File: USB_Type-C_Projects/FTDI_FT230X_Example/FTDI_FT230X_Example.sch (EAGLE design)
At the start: 52 parts, among them J1 105450-0101, J2 MF-CON-2.54mm-01x03, J3 MF-CON-2.54mm-01x02, J4 MF-CON-2.54mm-01x05, J5 MF-CON-2.54mm-01x03, J6 MF-CON-2.54mm-01x05, U1 FT230XQ-R, U2 IP4234CZ6,125, U3 IRLML6401TRPBF, U4 NCP1117LPST33T3G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

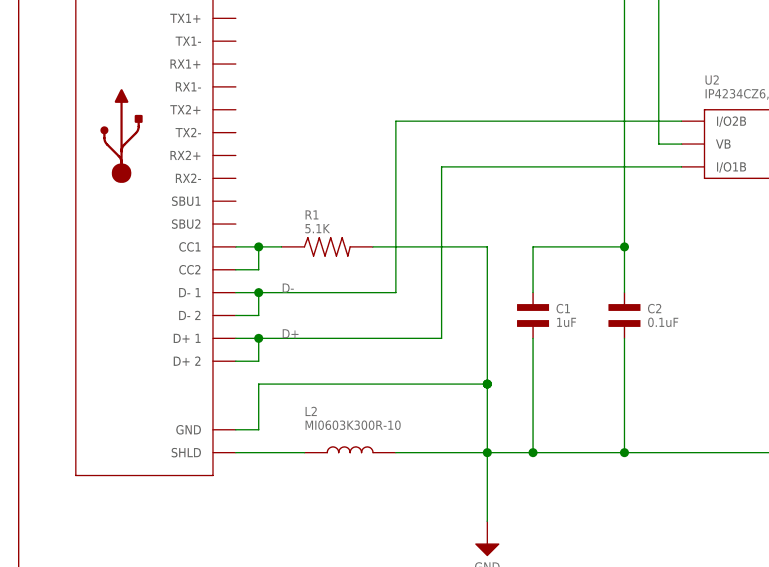
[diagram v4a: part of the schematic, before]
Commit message: updated with two (2 :O ) CC resistors
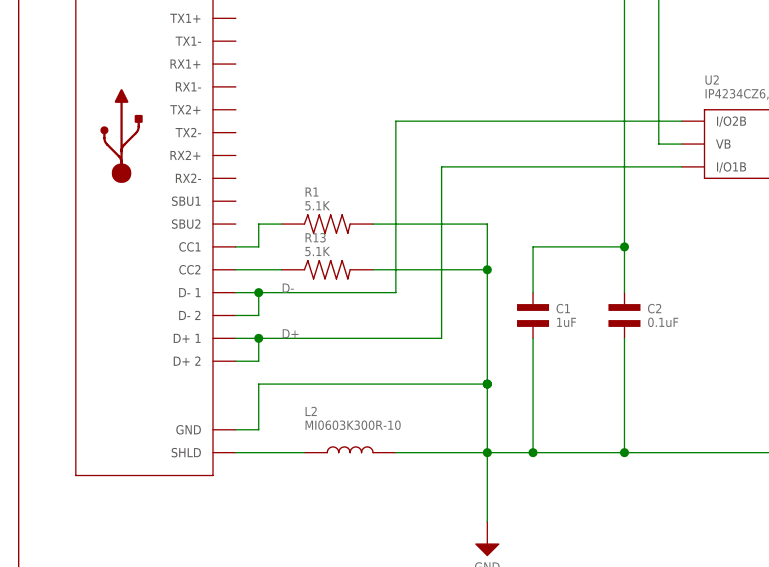
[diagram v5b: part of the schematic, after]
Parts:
- added R13: 5.1K, MF_Passives:RESISTOR_0603
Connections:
- removed net CC1/1: J1.CC1, J1.CC2, R1.P$1
- new net CC1: J1.CC1, R1.P$1
- new net CC2: J1.CC2, R13.P$1
- net GND: now also R13.P$2
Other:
- moved on the sheet: R1
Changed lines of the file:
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@@
 <attribute name="POPULATE" value="0"/>
+</part>
+<part name="R13" library="MF_Passives" deviceset="RESISTOR" device="_0603" value="5.1K">
+<attribute name="MPN" value="ERJ-3EKF5101V"/>
 </part>
 </parts>
@@
 <attribute name="VALUE" x="46.99" y="168.91" size="1.016" layer="96" font="vector" align="center"/>
 </instance>
-<instance part="R1" gate="G$1" x="34.29" y="128.27" smashed="yes" rot="R90">
-<attribute name="NAME" x="31.75" y="132.334" size="1.016" layer="95" font="vector" align="top-left"/>
-<attribute name="VALUE" x="31.75" y="129.794" size="1.016" layer="96" font="vector"/>
+<instance part="R1" gate="G$1" x="34.29" y="130.81" smashed="yes" rot="R90">
+<attribute name="NAME" x="31.75" y="134.874" size="1.016" layer="95" font="vector" align="top-left"/>
+<attribute name="VALUE" x="31.75" y="132.334" size="1.016" layer="96" font="vector"/>
 </instance>
 <instance part="R2" gate="G$1" x="115.57" y="143.51" smashed="yes" rot="R90">
@@
 <attribute name="LABEL02" x="285.75" y="54.61" size="1.016" layer="97" font="vector" align="center-left"/>
 </instance>
+<instance part="R13" gate="G$1" x="34.29" y="125.73" smashed="yes" rot="R90">
+<attribute name="NAME" x="31.75" y="129.794" size="1.016" layer="95" font="vector" align="top-left"/>
+<attribute name="VALUE" x="31.75" y="127.254" size="1.016" layer="96" font="vector"/>
+</instance>
 </instances>
 <busses>
@@
 <junction x="52.07" y="113.03"/>
 <wire x1="52.07" y1="113.03" x2="26.67" y2="113.03" width="0.1524" layer="91"/>
-<wire x1="39.37" y1="128.27" x2="52.07" y2="128.27" width="0.1524" layer="91"/>
-<wire x1="52.07" y1="128.27" x2="52.07" y2="113.03" width="0.1524" layer="91"/>
+<wire x1="39.37" y1="130.81" x2="52.07" y2="130.81" width="0.1524" layer="91"/>
+<wire x1="52.07" y1="130.81" x2="52.07" y2="125.73" width="0.1524" layer="91"/>
 <junction x="52.07" y="113.03"/>
+<wire x1="52.07" y1="125.73" x2="52.07" y2="113.03" width="0.1524" layer="91"/>
 <wire x1="41.91" y1="105.41" x2="52.07" y2="105.41" width="0.1524" layer="91"/>
 <wire x1="52.07" y1="105.41" x2="52.07" y2="113.03" width="0.1524" layer="91"/>
@@
 <wire x1="93.98" y1="139.7" x2="93.98" y2="105.41" width="0.1524" layer="91"/>
 <junction x="93.98" y="105.41"/>
+<pinref part="R13" gate="G$1" pin="P$2"/>
+<wire x1="39.37" y1="125.73" x2="52.07" y2="125.73" width="0.1524" layer="91"/>
+<junction x="52.07" y="125.73"/>
 </segment>
 <segment>
@@
 </segment>
 </net>
-<net name="CC1/1" class="0">
+<net name="CC1" class="0">
 <segment>
 <pinref part="J1" gate="G$1" pin="CC1"/>
 <wire x1="24.13" y1="128.27" x2="26.67" y2="128.27" width="0.1524" layer="91"/>
-<wire x1="26.67" y1="128.27" x2="26.67" y2="125.73" width="0.1524" layer="91"/>
-<pinref part="J1" gate="G$1" pin="CC2"/>
-<wire x1="26.67" y1="125.73" x2="24.13" y2="125.73" width="0.1524" layer="91"/>
-<wire x1="26.67" y1="128.27" x2="29.21" y2="128.27" width="0.1524" layer="91"/>
-<junction x="26.67" y="128.27"/>
+<wire x1="26.67" y1="128.27" x2="26.67" y2="130.81" width="0.1524" layer="91"/>
+<wire x1="26.67" y1="130.81" x2="29.21" y2="130.81" width="0.1524" layer="91"/>
 <pinref part="R1" gate="G$1" pin="P$1"/>
 </segment>
@@
 </segment>
 </net>
+<net name="CC2" class="0">
+<segment>
+<pinref part="J1" gate="G$1" pin="CC2"/>
+<pinref part="R13" gate="G$1" pin="P$1"/>
+<wire x1="24.13" y1="125.73" x2="29.21" y2="125.73" width="0.1524" layer="91"/>
+</segment>
+</net>
